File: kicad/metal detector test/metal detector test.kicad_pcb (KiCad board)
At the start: 2 copper layers, 72.6 x 125 mm, 110 parts, among them J1 3.5mm audio jack TRS, Q1 PNP, Q2 NPN, SW1 SW_SPST, SW10 SW_SPST, SW2 SW_SPST, SW3 SW_SPST, SW4 SW_SPST, SW5 SW_SPST, SW6 SW_SPST, SW7 SW_SPST, SW8 SW_SPST, SW9 SW_SPST, U1 op amp (higher voltage), U10 3.3v lin reg, U11 lp filter, U12 op amp (lower voltage), U2 nucleo-32 uC module, U3 9v lin reg, U4 5v lin reg, U5 3.3v lin reg, U6 audio amp, U7 lp filter, U8 switch debounce, U9 5v lin reg

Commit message: small changes
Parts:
- C13, U8: moved to F.Cu
- moved DS1 43.2 mm to (96.0, 43.9), turned to -90 degrees
- moved R10 33.4 mm to (53.1, 170.2)
- moved R7 33.4 mm to (49.3, 170.2)
- moved C13 24.6 mm to (70.4, 88.4), turned to 90 degrees
- moved U8 9.30 mm to (75.9, 96.5), turned to -90 degrees
- moved C10 4.10 mm to (97.5, 159.3)
- moved C9 4.10 mm to (97.5, 163.1)
- moved U4 4.10 mm to (91.7, 161.0)
- moved U2 3.56 mm to (95.5, 146.1)

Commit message: Figuring out oled and battery holder placement
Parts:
- removed C31: 100n, Capacitor_SMD:C_0805_2012Metric_Pad1.18x1.45mm_HandSolder
- removed the C4 at (104.9, 92.1)
- added N1: battery holder, allen footprints:106990288_18650_x3_battery_holder, F.Cu at (5.88, 0.00)
- moved C24 100.7 mm to (65.1, 67.6)
- moved C28 100.7 mm to (49.3, 61.8)
- moved C29 100.7 mm to (12.4, 48.5)
- moved C5 100.7 mm to (59.2, 17.9)
- moved C6 100.7 mm to (46.8, 78.1)
- moved C8 100.7 mm to (37.7, 82.1)
- moved C9 100.7 mm to (37.7, 78.2)
- moved H2 100.7 mm to (2.14, 76.0)
- moved LS1 100.7 mm to (67.4, 78.1)
- moved LS2 100.7 mm to (50.4, 72.8)
- moved R11 100.7 mm to (69.4, 17.9)
- moved U2 100.7 mm to (35.6, 65.0)
- moved BT1 100.7 mm to (4.67, 72.5)
- moved C1 100.7 mm to (53.2, 27.6)
- moved C10 100.7 mm to (48.1, 42.8)
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- renumbered C11 to C10, C12 to C11, C13 to C12, C14 to C13, C15 to C14, C16 to C15, C17 to C16, C18 to C17, C19 to C18, C20 to C19, C21 to C20, C22 to C21, C23 to C22, C24 to C23, C25 to C24, C26 to C25, C27 to C26, C28 to C27, C29 to C28, C30 to C29, C5 to C4, C6 to C5, C7 to C6, C8 to C7, C9 to C8, C10 to C9, LS2 to LS1, LS1 to LS2
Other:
- board size 72.6 x 125 mm -> 72.6 x 88.9 mm

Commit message: most of the placement done
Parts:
- moved G*** 105.7 mm to (-35.8, 99.8)
- moved N1 92.6 mm to (-86.7, -2.19)
- moved JP2 69.8 mm to (20.2, 56.4), turned to 180 degrees
- moved H1 41.4 mm to (95.8, 19.3)
- moved H8 41.4 mm to (91.7, 32.5)
- moved H3 41.4 mm to (95.8, 27.8)
- moved H4 41.4 mm to (95.8, 31.8)
- moved H5 41.4 mm to (95.8, 35.8)
- moved H6 41.4 mm to (91.7, 23.9)
- moved H7 41.4 mm to (91.7, 28.2)
- moved H9 41.4 mm to (91.7, 36.7)
- moved R10 34.3 mm to (2.52, 95.8)
- moved R7 34.3 mm to (-1.29, 95.8)
- moved TP3 30.0 mm to (90.7, 81.8)
- moved TP4 30.0 mm to (90.7, 63.5)
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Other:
- board size 72.6 x 88.9 mm -> 82.8 x 88.9 mm

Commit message: working on part positions still
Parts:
- moved H5 88.7 mm to (7.11, 37.6)
- moved H4 64.1 mm to (59.4, 84.6)
- moved JP2 36.8 mm to (25.9, 20.1)
- moved H3 32.1 mm to (77.7, 54.4)
- moved R10 29.5 mm to (26.4, 78.5)
- moved R7 29.5 mm to (22.6, 78.5)
- moved H1 21.3 mm to (74.7, 16.8)
- moved L_TX1 10.2 mm to (70.6, 18.0)
- moved JP4 7.12 mm to (37.3, 7.37), turned to 90 degrees
- moved JP3 7.08 mm to (39.9, 7.37)
- moved L_TX2 6.99 mm to (78.0, 46.7), turned to 180 degrees
- moved TP8 6.92 mm to (8.38, 51.1)
- moved N1 4.88 mm to (-83.7, -6.00)
- moved FB1 4.66 mm to (38.6, 4.83), turned to 180 degrees
- moved U2 3.82 mm to (41.1, 68.3)
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- renumbered SW2 to SW0, SW3 to SW1, SW1 to SW10, SW4 to SW2, SW5 to SW3, SW6 to SW4, SW7 to SW5, SW8 to SW6, SW9 to SW7, SW10 to SW8
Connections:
- JP2 pad 2: SW8 -> SW6
- U2 pad 1: SW0 -> SW5
- U2 pad 2: SW1 -> SW4
- U2 pad 20: SW6 -> SW8
- U2 pad 5: SW2 -> SW3
- U2 pad 6: SW3 -> SW2
- U2 pad 7: SW4 -> SW1
- U2 pad 8: SW5 -> SW0

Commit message: Realized that I was accidentially using a pin required to use the external 8 MHz MCO xtal signal passed from the debugger chip, changed to another one.
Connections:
- U2 pad 10: Net-(DS1-DC) -> /(MCO)
- U2 pad 15: unconnected-(U2-PB_4-Pad15) -> Net-(DS1-DC)
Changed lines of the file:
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@@
   (net 47 "Net-(U6A-+)")
   (net 48 "Net-(U7-OUT)")
-  (net 49 "Net-(DS1-VCC)")
+  (net 49 "Net-(#FLG01-pwr)")
   (net 50 "Net-(C16-Pad1)")
   (net 51 "Net-(C17-Pad2)")
@@
   (net 69 "Net-(U12B-+)")
   (net 70 "unconnected-(U2-NRST-Pad3)")
-  (net 71 "unconnected-(U2-PB_4-Pad15)")
+  (net 71 "/(MCO)")
   (net 72 "unconnected-(U2-NRST-Pad28)")
   (net 73 "Net-(C25-Pad1)")
@@
       (net 60 "Net-(JP3-B)") (pintype "passive"))
     (pad "2" smd roundrect (at 1.15 0 180) (size 1.05 1.2) (layers "F.Cu" "F.Paste" "F.Mask") (roundrect_rratio 0.238095)
-      (net 49 "Net-(DS1-VCC)") (pintype "passive"))
+      (net 49 "Net-(#FLG01-pwr)") (pintype "passive"))
     (model "${KICAD6_3DMODEL_DIR}/Inductor_SMD.3dshapes/L_0805_2012Metric.wrl"
       (offset (xyz 0 0 0))
@@
       (net 15 "Net-(DS1-CS)") (pinfunction "PB_1") (pintype "bidirectional"))
     (pad "10" thru_hole oval (at 0 22.86 180) (size 1.6 1.6) (drill 1) (layers "*.Cu" "*.Mask")
-      (net 14 "Net-(DS1-DC)") (pinfunction "PF_0") (pintype "bidirectional"))
+      (net 71 "/(MCO)") (pinfunction "PF_0") (pintype "bidirectional"))
     (pad "11" thru_hole oval (at 0 25.4 180) (size 1.6 1.6) (drill 1) (layers "*.Cu" "*.Mask")
       (net 13 "Net-(DS1-RES)") (pinfunction "PF_1") (pintype "bidirectional"))
@@
       (net 12 "Net-(DS1-SDA)") (pinfunction "PB_5") (pintype "bidirectional"))
     (pad "15" thru_hole oval (at 0 35.56 180) (size 1.6 1.6) (drill 1) (layers "*.Cu" "*.Mask")
-      (net 71 "unconnected-(U2-PB_4-Pad15)") (pinfunction "PB_4") (pintype "bidirectional"))
+      (net 14 "Net-(DS1-DC)") (pinfunction "PB_4") (pintype "bidirectional"))
     (pad "16" thru_hole oval (at 15.24 35.56 180) (size 1.6 1.6) (drill 1) (layers "*.Cu" "*.Mask")
       (net 11 "Net-(DS1-SCK)") (pinfunction "PB_3") (pintype "bidirectional"))
@@
       (stroke (width 0.1) (type solid)) (layer "F.Fab"))
     (pad "1" smd roundrect (at -1.0375 0 180) (size 1.175 1.45) (layers "F.Cu" "F.Paste" "F.Mask") (roundrect_rratio 0.212766)
-      (net 49 "Net-(DS1-VCC)") (pintype "passive"))
+      (net 49 "Net-(#FLG01-pwr)") (pintype "passive"))
     (pad "2" smd roundrect (at 1.0375 0 180) (size 1.175 1.45) (layers "F.Cu" "F.Paste" "F.Mask") (roundrect_rratio 0.212766)
       (net 2 "GNDA") (pintype "passive"))
@@
       (net 2 "GNDA") (pinfunction "GND") (pintype "power_in"))
     (pad "2" thru_hole oval locked (at 0 5.08 270) (size 1.7 1.7) (drill 1) (layers "*.Cu" "*.Mask")
-      (net 49 "Net-(DS1-VCC)") (pinfunction "VCC") (pintype "power_in"))
+      (net 49 "Net-(#FLG01-pwr)") (pinfunction "VCC") (pintype "power_in"))
     (pad "3" thru_hole oval locked (at 0 2.54 270) (size 1.7 1.7) (drill 1) (layers "*.Cu" "*.Mask")
       (net 11 "Net-(DS1-SCK)") (pinfunction "SCK") (pintype "input"))

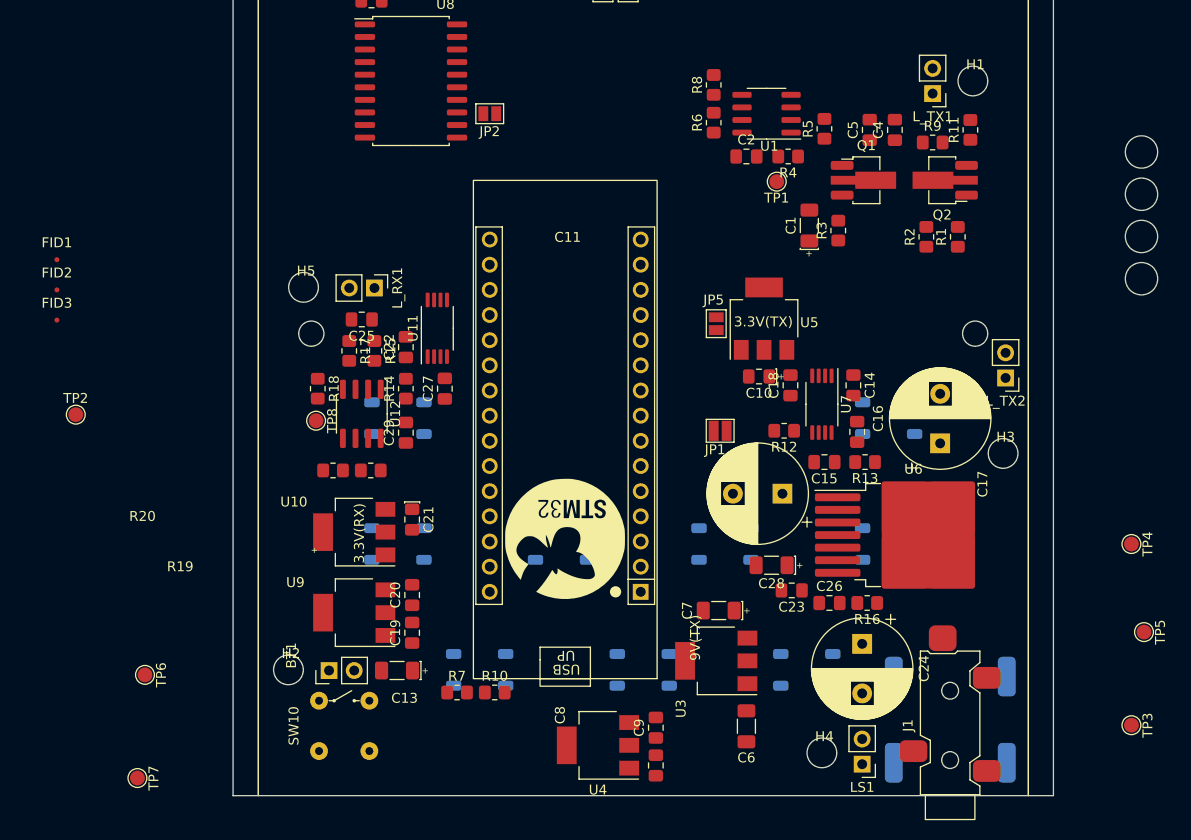
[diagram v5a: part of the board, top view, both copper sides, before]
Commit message: considering filtering the audio output
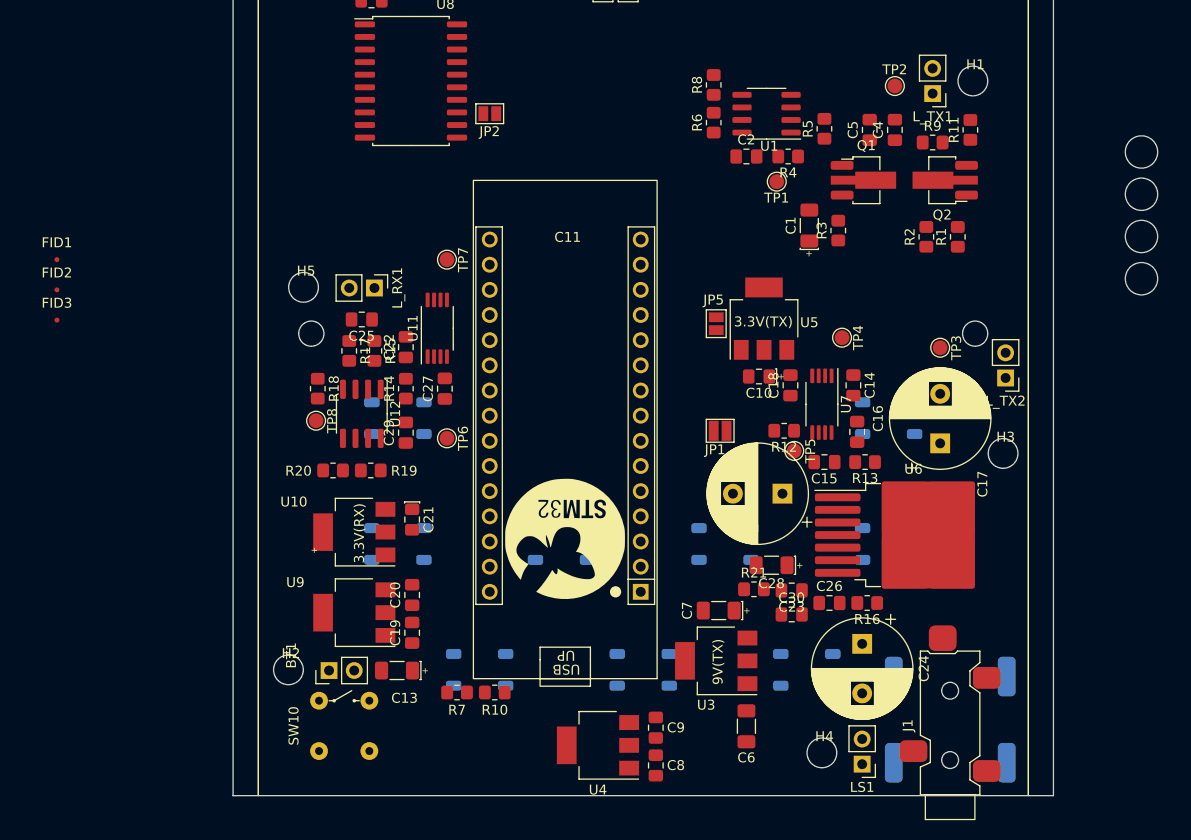
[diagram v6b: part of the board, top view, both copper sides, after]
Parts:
- added C30: 100n, Capacitor_SMD:C_0805_2012Metric_Pad1.18x1.45mm_HandSolder, F.Cu at (56.4, 70.6)
- added R21: 100, Resistor_SMD:R_0805_2012Metric_Pad1.20x1.40mm_HandSolder, F.Cu at (52.6, 68.1)
- moved TP2 89.1 mm to (66.8, 17.3)
- moved TP7 60.9 mm to (21.6, 34.8)
- moved TP3 42.7 mm to (71.4, 43.7)
- moved TP5 39.8 mm to (56.6, 54.1)
- moved TP6 38.7 mm to (21.6, 52.8)
- moved TP4 35.9 mm to (61.5, 42.7)
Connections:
- C23 pad 2: AUDIO -> Net-(C23-Pad2)
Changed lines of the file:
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@@
   (net 75 "Net-(SW0-B)")
   (net 76 "Net-(SW1-B)")
+  (net 77 "Net-(C23-Pad2)")
   (footprint "Resistor_SMD:R_0805_2012Metric_Pad1.20x1.40mm_HandSolder" placed (layer "F.Cu")
     (at 10.09 56.0755 180)
@@
     (property "ki_keywords" "r resistor")
     (attr smd)
-    (fp_text reference "R20" (at 19.234 -4.6305) (layer "F.SilkS")
+    (fp_text reference "R20" (at 3.486 -0.0585) (layer "F.SilkS")
         (effects (font (size 1 1) (thickness 0.15)))
     )
@@
     (pad "" np_thru_hole circle (at 0 0) (size 3 3) (drill 3) (layers "F&B.Cu" "*.Mask"))
   )
+  (footprint "Resistor_SMD:R_0805_2012Metric_Pad1.20x1.40mm_HandSolder" (layer "F.Cu")
+    (at 52.578 68.072)
+    (descr "Resistor SMD 0805 (2012 Metric), square (rectangular) end terminal, IPC_7351 nominal with elongated pad for handsoldering. (Body size source: IPC-SM-782 page 72, https://www.pcb-3d.com/wordpress/wp-content/uploads/ipc-sm-782a_amendment_1_and_2.pdf), generated with kicad-footprint-generator")
+    (tags "resistor handsolder")
+    (property "Sheetfile" "metal detector test.kicad_sch")
+    (property "Sheetname" "")
+    (property "ki_description" "Resistor, small US symbol")
+    (property "ki_keywords" "r resistor")
+    (attr smd)
+    (fp_text reference "R21" (at 0 -1.65) (layer "F.SilkS")
+        (effects (font (size 1 1) (thickness 0.15)))
+    )
+    (fp_text value "100" (at 0 1.65) (layer "F.Fab")
+        (effects (font (size 1 1) (thickness 0.15)))
+    )
+    (fp_text user "${REFERENCE}" (at 0 0) (layer "F.Fab")
+        (effects (font (size 0.5 0.5) (thickness 0.08)))
+    )
+    (fp_line (start -0.227064 -0.735) (end 0.227064 -0.735)
+      (stroke (width 0.12) (type solid)) (layer "F.SilkS"))
+    (fp_line (start -0.227064 0.735) (end 0.227064 0.735)
+      (stroke (width 0.12) (type solid)) (layer "F.SilkS"))
+    (fp_line (start -1.85 -0.95) (end 1.85 -0.95)
+      (stroke (width 0.05) (type solid)) (layer "F.CrtYd"))
+    (fp_line (start -1.85 0.95) (end -1.85 -0.95)
+      (stroke (width 0.05) (type solid)) (layer "F.CrtYd"))
+    (fp_line (start 1.85 -0.95) (end 1.85 0.95)
+      (stroke (width 0.05) (type solid)) (layer "F.CrtYd"))
+    (fp_line (start 1.85 0.95) (end -1.85 0.95)
+      (stroke (width 0.05) (type solid)) (layer "F.CrtYd"))
+    (fp_line (start -1 -0.625) (end 1 -0.625)
+      (stroke (width 0.1) (type solid)) (layer "F.Fab"))
+    (fp_line (start -1 0.625) (end -1 -0.625)
+      (stroke (width 0.1) (type solid)) (layer "F.Fab"))
+    (fp_line (start 1 -0.625) (end 1 0.625)
+      (stroke (width 0.1) (type solid)) (layer "F.Fab"))
+    (fp_line (start 1 0.625) (end -1 0.625)
+      (stroke (width 0.1) (type solid)) (layer "F.Fab"))
+    (pad "1" smd roundrect (at -1 0) (size 1.2 1.4) (layers "F.Cu" "F.Paste" "F.Mask") (roundrect_rratio 0.208333)
+      (net 10 "AUDIO") (pintype "passive"))
+    (pad "2" smd roundrect (at 1 0) (size 1.2 1.4) (layers "F.Cu" "F.Paste" "F.Mask") (roundrect_rratio 0.208333)
+      (net 77 "Net-(C23-Pad2)") (pintype "passive"))
+    (model "${KICAD6_3DMODEL_DIR}/Resistor_SMD.3dshapes/R_0805_2012Metric.wrl"
+      (offset (xyz 0 0 0))
+      (scale (xyz 1 1 1))
+      (rotate (xyz 0 0 0))
+    )
+  )
   (footprint "Capacitor_SMD:C_0805_2012Metric_Pad1.18x1.45mm_HandSolder" placed (layer "F.Cu")
     (at 64.262 21.702 90)
@@
   )
   (footprint "TestPoint:TestPoint_Pad_D1.5mm" (layer "F.Cu")
-    (at 90.678 63.5 -90)
+    (at 61.468 42.672 -90)
     (descr "SMD pad as test Point, diameter 1.5mm")
     (tags "test point SMD pad")
@@
     (pad "" np_thru_hole circle (at 0 0) (size 3 3) (drill 3) (layers "F&B.Cu" "*.Mask"))
   )
+  (footprint "Capacitor_SMD:C_0805_2012Metric_Pad1.18x1.45mm_HandSolder" (layer "F.Cu")
+    (at 56.388 70.612)
+    (descr "Capacitor SMD 0805 (2012 Metric), square (rectangular) end terminal, IPC_7351 nominal with elongated pad for handsoldering. (Body size source: IPC-SM-782 page 76, https://www.pcb-3d.com/wordpress/wp-content/uploads/ipc-sm-782a_amendment_1_and_2.pdf, https://docs.google.com/spreadsheets/d/1BsfQQcO9C6DZCsRaXUlFlo91Tg2WpOkGARC1WS5S8t0/edit?usp=sharing), generated with kicad-footprint-generator")
+    (tags "capacitor handsolder")
+    (property "Sheetfile" "metal detector test.kicad_sch")
+    (property "Sheetname" "")
+    (property "ki_description" "Unpolarized capacitor, small symbol")
+    (property "ki_keywords" "capacitor cap")
+    (attr smd)
+    (fp_text reference "C30" (at 0 -1.68) (layer "F.SilkS")
+        (effects (font (size 1 1) (thickness 0.15)))
+    )
+    (fp_text value "100n" (at 0 1.68) (layer "F.Fab")
+        (effects (font (size 1 1) (thickness 0.15)))
+    )
+    (fp_text user "${REFERENCE}" (at 0 0) (layer "F.Fab")
+        (effects (font (size 0.5 0.5) (thickness 0.08)))
+    )
+    (fp_line (start -0.261252 -0.735) (end 0.261252 -0.735)
+      (stroke (width 0.12) (type solid)) (layer "F.SilkS"))
+    (fp_line (start -0.261252 0.735) (end 0.261252 0.735)
+      (stroke (width 0.12) (type solid)) (layer "F.SilkS"))
+    (fp_line (start -1.88 -0.98) (end 1.88 -0.98)
+      (stroke (width 0.05) (type solid)) (layer "F.CrtYd"))
+    (fp_line (start -1.88 0.98) (end -1.88 -0.98)
+      (stroke (width 0.05) (type solid)) (layer "F.CrtYd"))
+    (fp_line (start 1.88 -0.98) (end 1.88 0.98)
+      (stroke (width 0.05) (type solid)) (layer "F.CrtYd"))
+    (fp_line (start 1.88 0.98) (end -1.88 0.98)
+      (stroke (width 0.05) (type solid)) (layer "F.CrtYd"))
+    (fp_line (start -1 -0.625) (end 1 -0.625)
+      (stroke (width 0.1) (type solid)) (layer "F.Fab"))
+    (fp_line (start -1 0.625) (end -1 -0.625)
+      (stroke (width 0.1) (type solid)) (layer "F.Fab"))
+    (fp_line (start 1 -0.625) (end 1 0.625)
+      (stroke (width 0.1) (type solid)) (layer "F.Fab"))
+    (fp_line (start 1 0.625) (end -1 0.625)
+      (stroke (width 0.1) (type solid)) (layer "F.Fab"))
+    (pad "1" smd roundrect (at -1.0375 0) (size 1.175 1.45) (layers "F.Cu" "F.Paste" "F.Mask") (roundrect_rratio 0.212766)
+      (net 77 "Net-(C23-Pad2)") (pintype "passive"))
+    (pad "2" smd roundrect (at 1.0375 0) (size 1.175 1.45) (layers "F.Cu" "F.Paste" "F.Mask") (roundrect_rratio 0.212766)
+      (net 2 "GNDA") (pintype "passive"))
+    (model "${KICAD6_3DMODEL_DIR}/Capacitor_SMD.3dshapes/C_0805_2012Metric.wrl"
+      (offset (xyz 0 0 0))
+      (scale (xyz 1 1 1))
+      (rotate (xyz 0 0 0))
+    )
+  )
   (footprint "Package_TO_SOT_SMD:SOT-223-3_TabPin2" placed (layer "F.Cu")
     (at 12.233 70.4265 180)
@@
       (net 47 "Net-(U6A-+)") (pintype "passive"))
     (pad "2" smd roundrect (at 1.0375 0 180) (size 1.175 1.45) (layers "F.Cu" "F.Paste" "F.Mask") (roundrect_rratio 0.212766)
-      (net 10 "AUDIO") (pintype "passive"))
+      (net 77 "Net-(C23-Pad2)") (pintype "passive"))
     (model "${KICAD6_3DMODEL_DIR}/Capacitor_SMD.3dshapes/C_0805_2012Metric.wrl"
       (offset (xyz 0 0 0))
@@
     (property "ki_keywords" "capacitor cap")
     (attr smd)
-    (fp_text reference "C9" (at 0 -1.68 90) (layer "F.SilkS")
+    (fp_text reference "C9" (at 0 2.032) (layer "F.SilkS")
         (effects (font (size 1 1) (thickness 0.15)))
     )
@@
   )
   (footprint "TestPoint:TestPoint_Pad_D1.5mm" (layer "F.Cu")
-    (at -15.875 50.443)
+    (at 66.802 17.272)
     (descr "SMD pad as test Point, diameter 1.5mm")
     (tags "test point SMD pad")
@@
     (property "ki_keywords" "REGULATOR LDO fixed positive")
     (attr smd)
-    (fp_text reference "U3" (at 3.556 -4.826 90) (layer "F.SilkS")
+    (fp_text reference "U3" (at 1.016 -4.46 180) (layer "F.SilkS")
         (effects (font (size 1 1) (thickness 0.15)))
     )
@@
     (property "ki_keywords" "r resistor")
     (attr smd)
-    (fp_text reference "R7" (at 0 -1.65) (layer "F.SilkS")
+    (fp_text reference "R7" (at 0 1.778) (layer "F.SilkS")
         (effects (font (size 1 1) (thickness 0.15)))
     )
@@
   )
   (footprint "TestPoint:TestPoint_Pad_D1.5mm" (layer "F.Cu")
-    (at -9.652 87.122 -90)
+    (at 21.59 34.798 -90)
     (descr "SMD pad as test Point, diameter 1.5mm")
     (tags "test point SMD pad")
@@
     (property "ki_keywords" "r resistor")
     (attr smd)
-    (fp_text reference "R10" (at 0 -1.65) (layer "F.SilkS")
+    (fp_text reference "R10" (at 0 1.778) (layer "F.SilkS")
         (effects (font (size 1 1) (thickness 0.15)))
     )
@@
   )
   (footprint "TestPoint:TestPoint_Pad_D1.5mm" (layer "F.Cu")
-    (at 90.678 81.788 -90)
+    (at 71.374 43.688 -90)
     (descr "SMD pad as test Point, diameter 1.5mm")
     (tags "test point SMD pad")
@@
   )
   (footprint "TestPoint:TestPoint_Pad_D1.5mm" (layer "F.Cu")
-    (at -8.89 76.708 -90)
+    (at 21.59 52.832 -90)
     (descr "SMD pad as test Point, diameter 1.5mm")
     (tags "test point SMD pad")
@@
     (property "ki_keywords" "r resistor")
     (attr smd)
-    (fp_text reference "R19" (at 19.234 -9.7105) (layer "F.SilkS")
+    (fp_text reference "R19" (at -3.372 -0.0585) (layer "F.SilkS")
         (effects (font (size 1 1) (thickness 0.15)))
     )
@@
   )
   (footprint "TestPoint:TestPoint_Pad_D1.5mm" (layer "F.Cu")
-    (at 91.948 72.39 -90)
+    (at 56.642 54.102 -90)
     (descr "SMD pad as test Point, diameter 1.5mm")
     (tags "test point SMD pad")
@@
     (property "ki_keywords" "capacitor cap")
     (attr smd)
-    (fp_text reference "C8" (at 5.08 -9.652 90) (layer "F.SilkS")
+    (fp_text reference "C8" (at 0 2.032 180) (layer "F.SilkS")
         (effects (font (size 1 1) (thickness 0.15)))
     )
@@
     (effects (font (size 1 1) (thickness 0.15)) (justify left bottom))
   )
-  (gr_text "9V(TX)" (at 47.244 75.296 90) (layer "F.SilkS")
+  (gr_text "9V(TX)" (at 49.53 77.724 90) (layer "F.SilkS")
     (effects (font (size 1 1) (thickness 0.15)) (justify left bottom))
   )
